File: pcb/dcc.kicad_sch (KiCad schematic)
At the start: 7 parts, among them J3 Screw_Terminal_01x08, J4 Screw_Terminal_01x02, U3 6N137, U4 LM339, U5 LM339, U6 LM339, U7 LM339

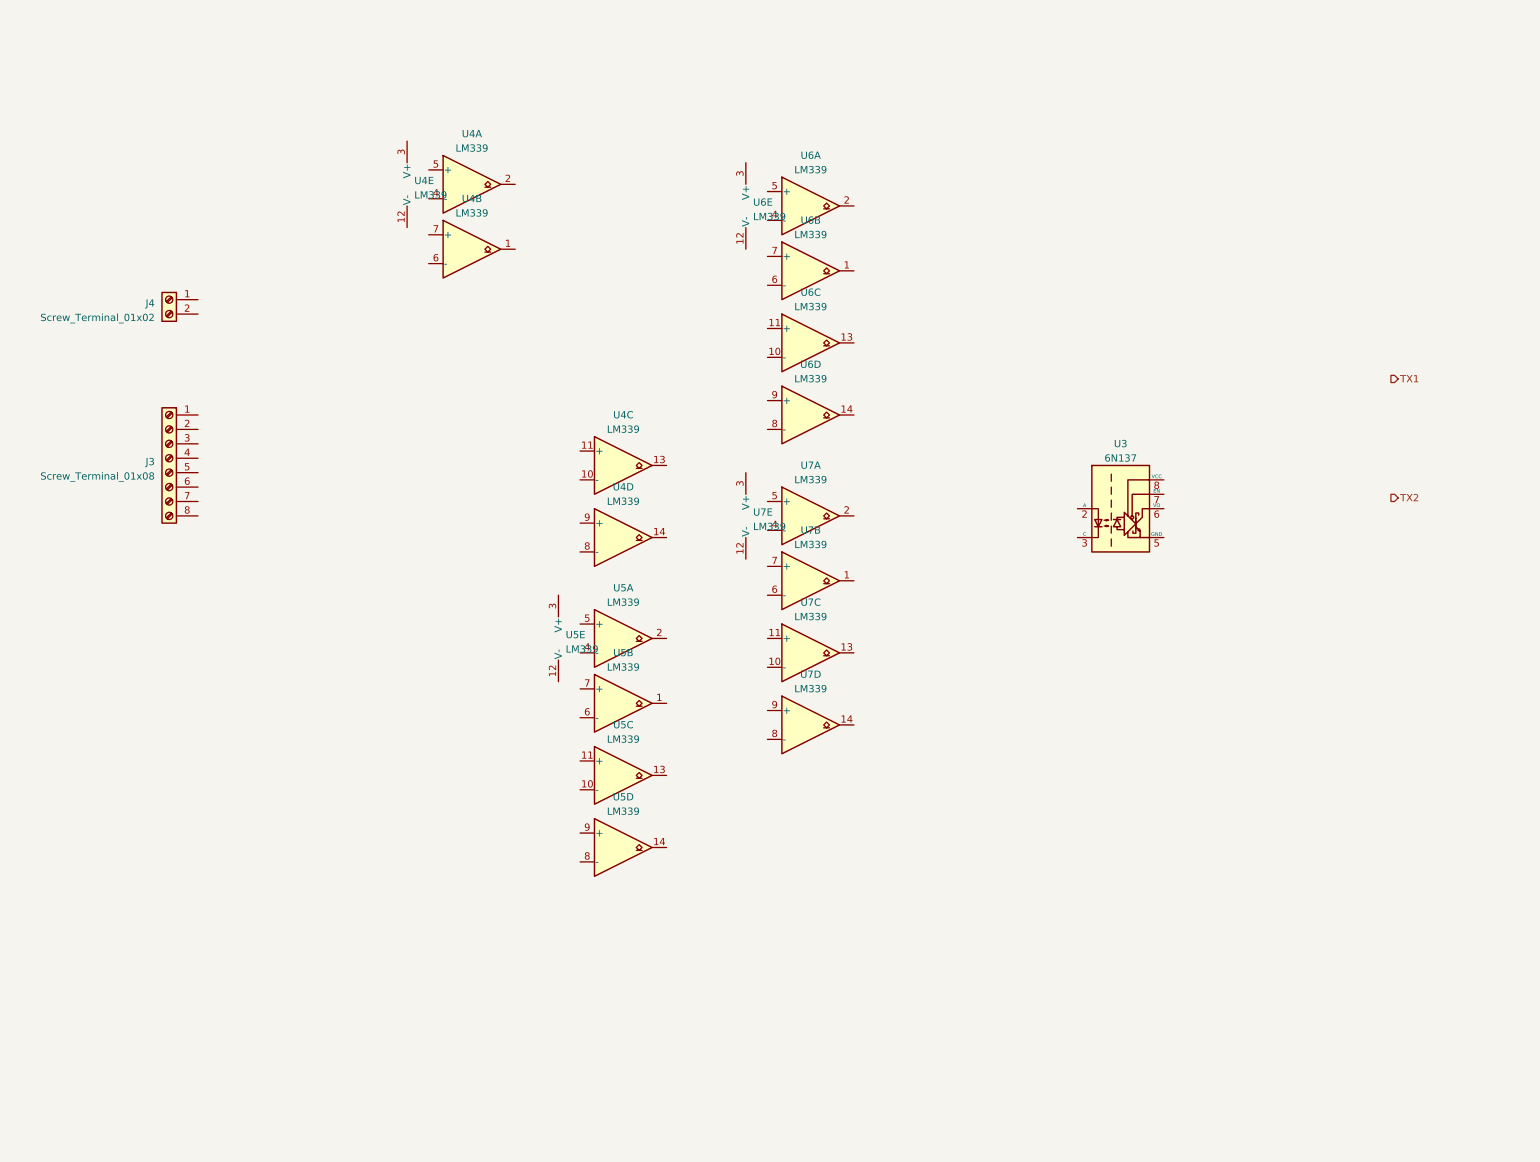
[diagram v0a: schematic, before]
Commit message: Wires adresses, add capacitors to MCU.
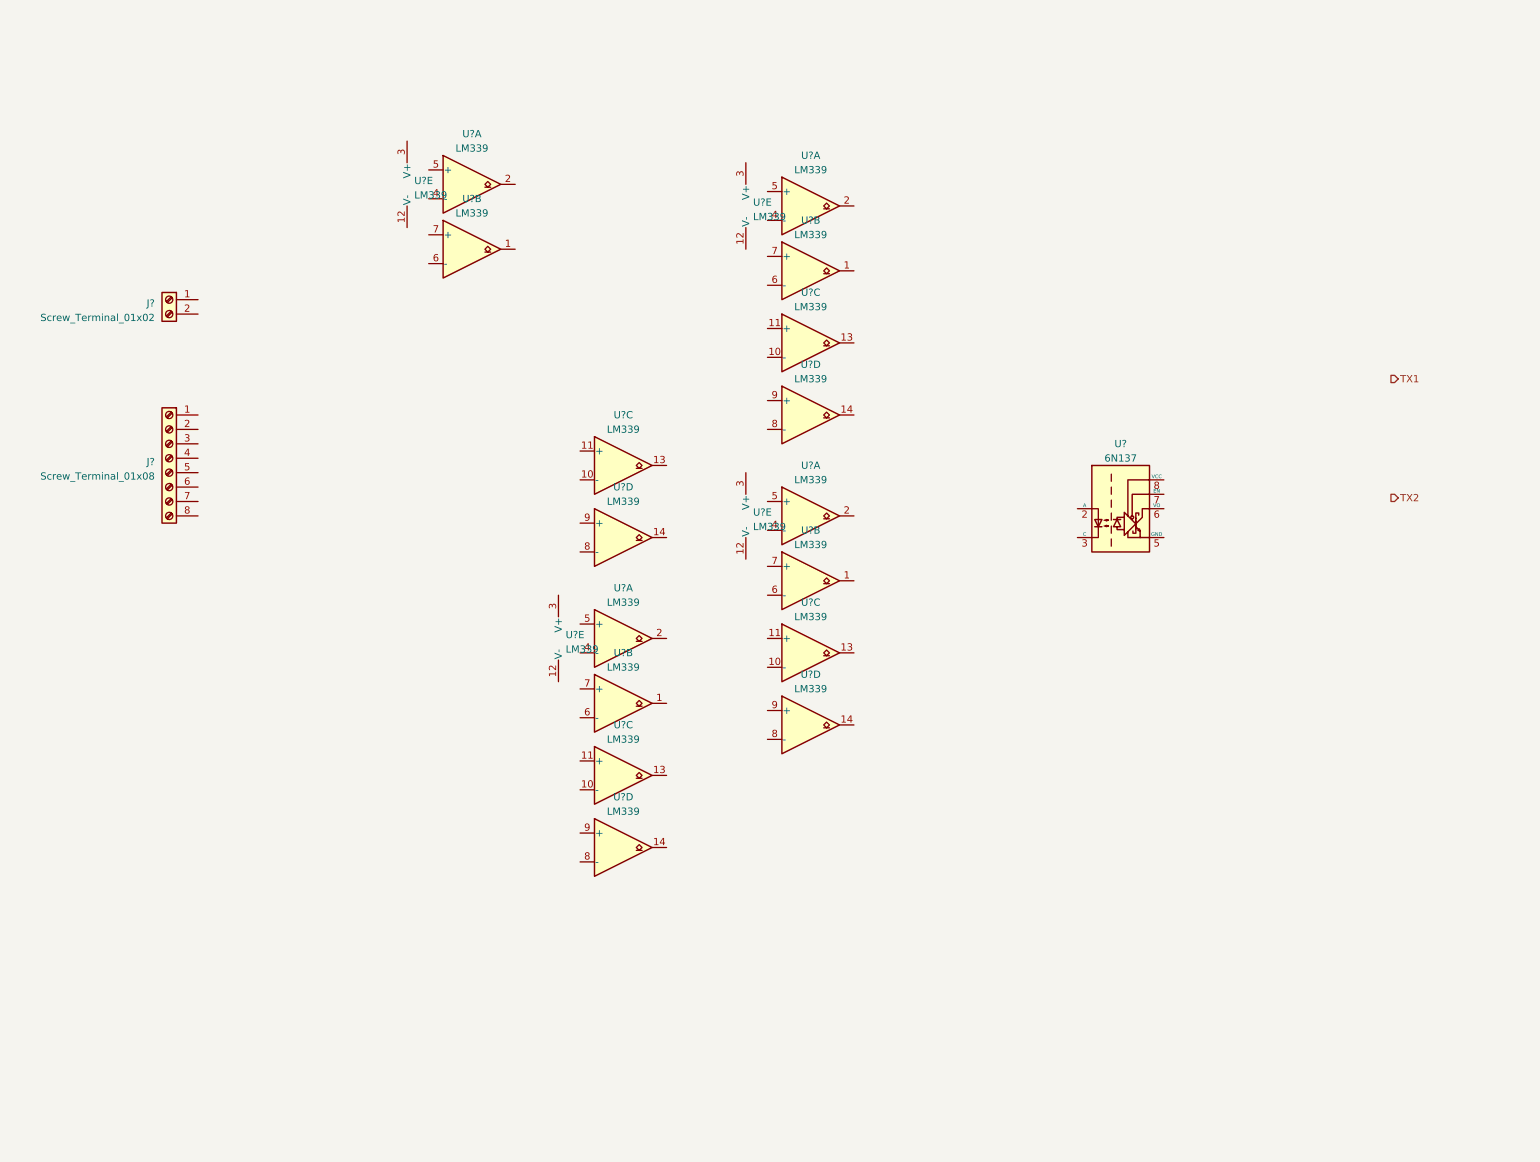
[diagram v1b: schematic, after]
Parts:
- renumbered J3 to J?, J4 to J?, U7 to U?, U5 to U?, U6 to U?, U4 to U?, U3 to U?

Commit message: Finished MTB part.
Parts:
- gave numbers to parts that had none: 7

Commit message: DCC WIP.
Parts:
- removed J2: Screw_Terminal_01x02, symbol Connector:Screw_Terminal_01x02
- removed J3: Screw_Terminal_01x08, symbol Connector:Screw_Terminal_01x08
- removed U7: 6N137, Package_DIP:DIP-8_W7.62mm, symbol Isolator:6N137
- added C14: C, symbol Device:C
- added R10: 1k, symbol Device:R
- added R11: 10k, symbol Device:R
- added R7, R8, R9: 1R5, symbol Device:R
- added U7: 4052, symbol 4xxx:4052
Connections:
- net TX1: now also U7.13 (X)
- net TX2: now also U7.3 (Y)
- net at U3.2: now also U3.1, R11.2
- net RC1: now reaches U3.4 (-)
- net RC1: now also U3.7 (+), R10.2
- net REF+: now reaches U3.5 (+)
- net REF-: now reaches U3.6 (-)
- new net +5VA: R11.1
- new net GNDA: R7.2, R8.2, R9.2
- new net J1: R10.1, R7.1
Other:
- note added: "Někde zde bude stabilizace napájení"
- moved on the sheet: U3A, U3B, U3C, U3D, U3E, U4A, U4B, U4C, U4D, U4E, U5A, U5B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

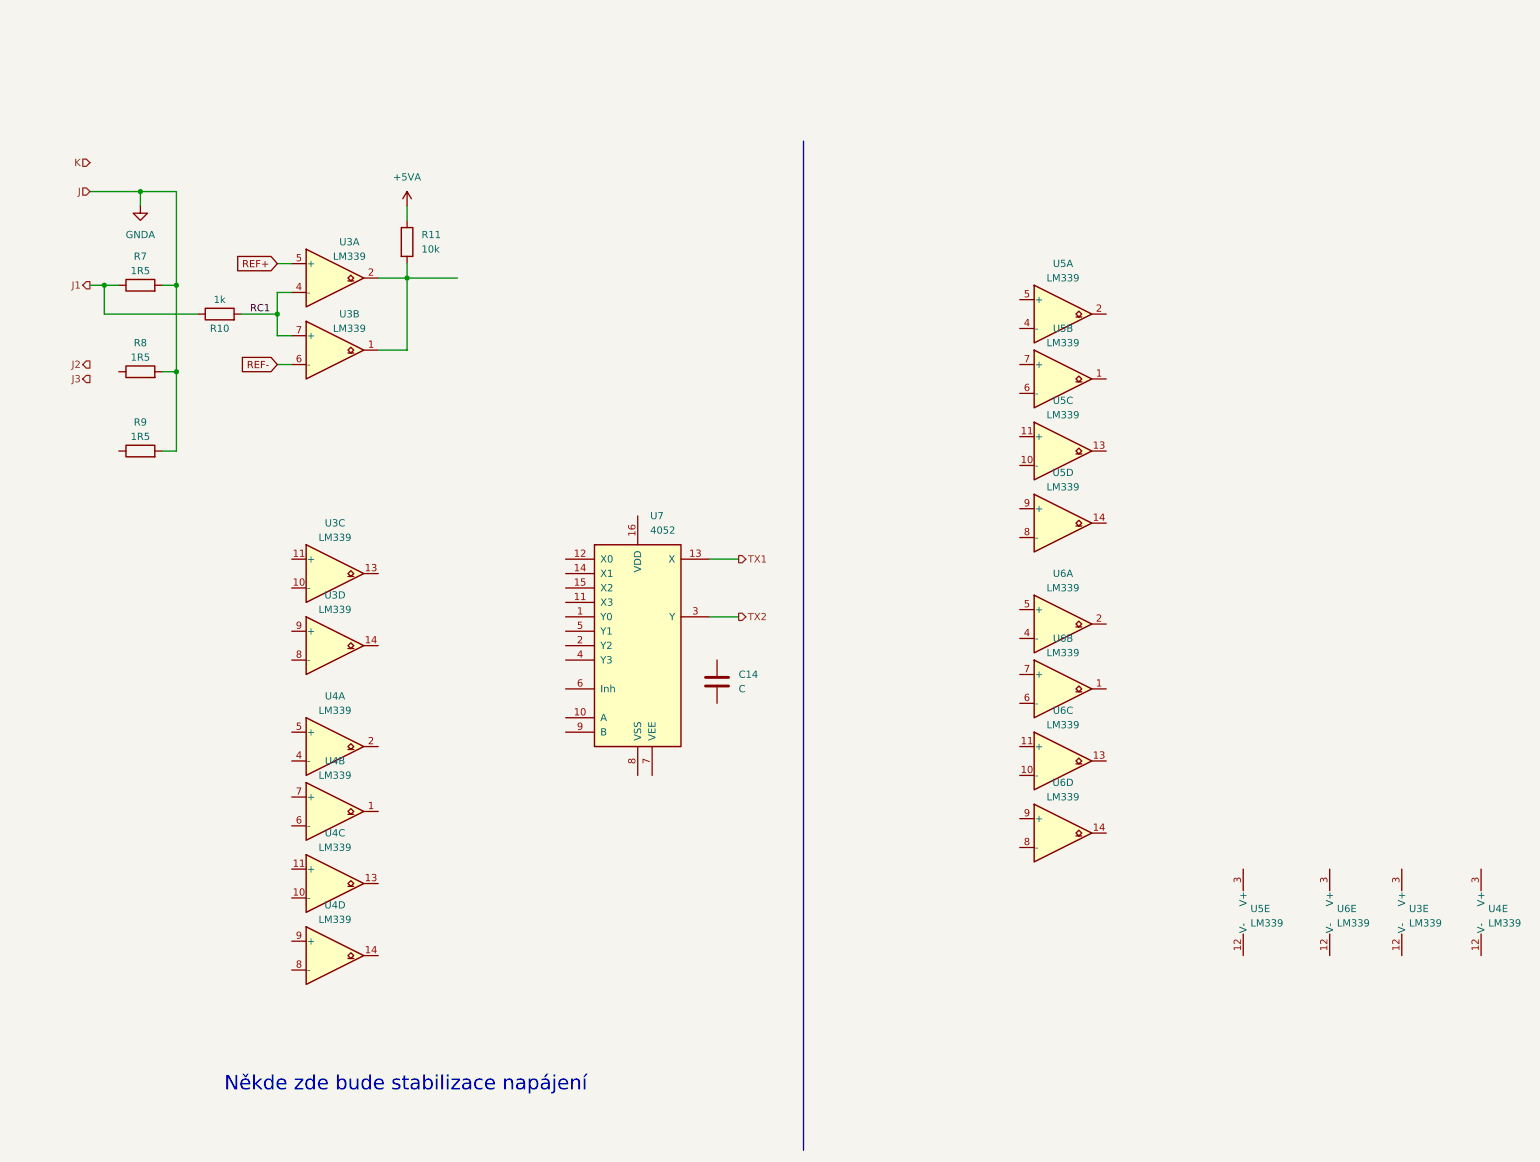
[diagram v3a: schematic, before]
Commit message: Some adjustments with comparators.
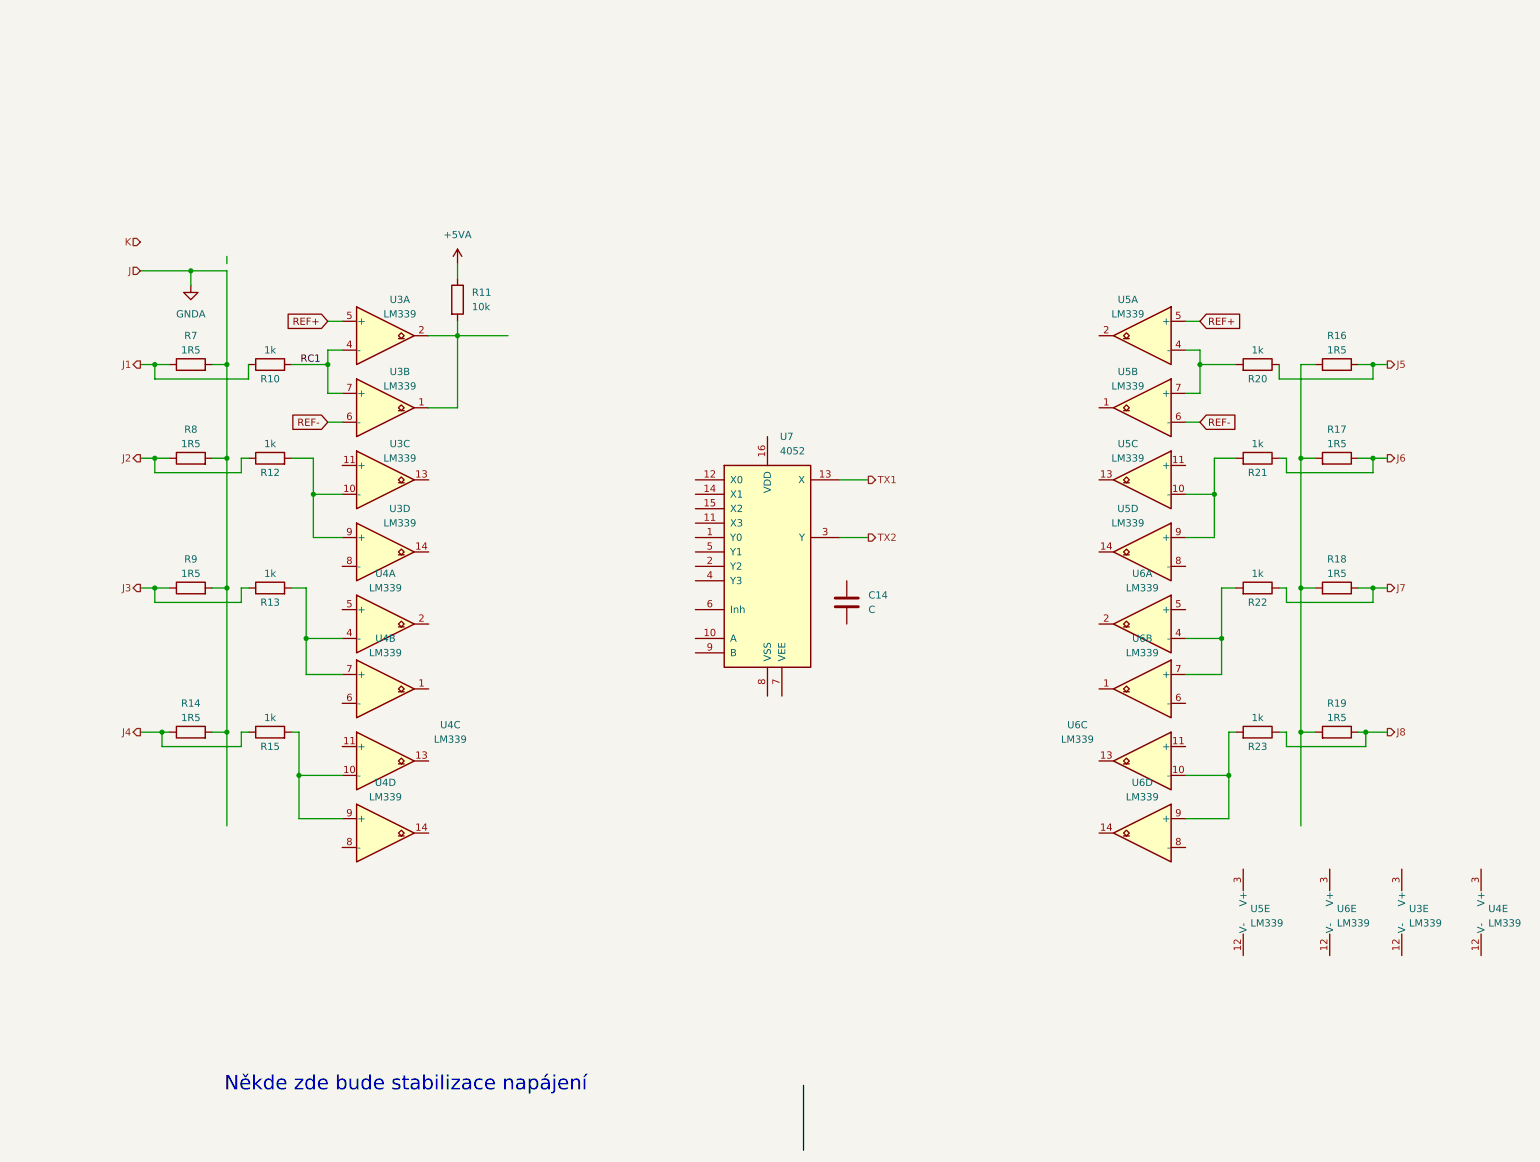
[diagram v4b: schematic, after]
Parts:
- added R12, R13, R15, R20, R21, R22, R23: 1k, symbol Device:R
- added R14, R16, R17, R18, R19: 1R5, symbol Device:R
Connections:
- net GNDA: now also R14.2
- net J2: now also R8.1, R12.1
- net J3: now also R9.1, R13.1
- net REF+: now also U5.5 (+)
- net REF-: now also U5.6 (-)
- net at U6.9 (+): now also U6.10 (-), R23.2
- net at U4.7 (+): now also U4.4 (-), R13.2
- net at U5.4 (-): now also U5.7 (+), R20.2
- net at U6.4 (-): now also U6.7 (+), R22.2
- net at U4.9 (+): now also U4.10 (-), R15.2
- net at U5.10 (-): now also U5.9 (+), R21.2
- net at U3.10 (-): now also U3.9 (+), R12.2
- new net: R16.2, R17.2, R18.2, R19.2
- new net J4: R14.1, R15.1
- new net J5: R16.1, R20.1
- new net J6: R17.1, R21.1
- new net J7: R18.1, R22.1
- new net J8: R19.1, R23.1
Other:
- moved on the sheet: C14, R10, R11, R7, R8, R9, U3A, U3B, U3C, U3D, U4A, U4B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

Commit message: Updated DCC part.
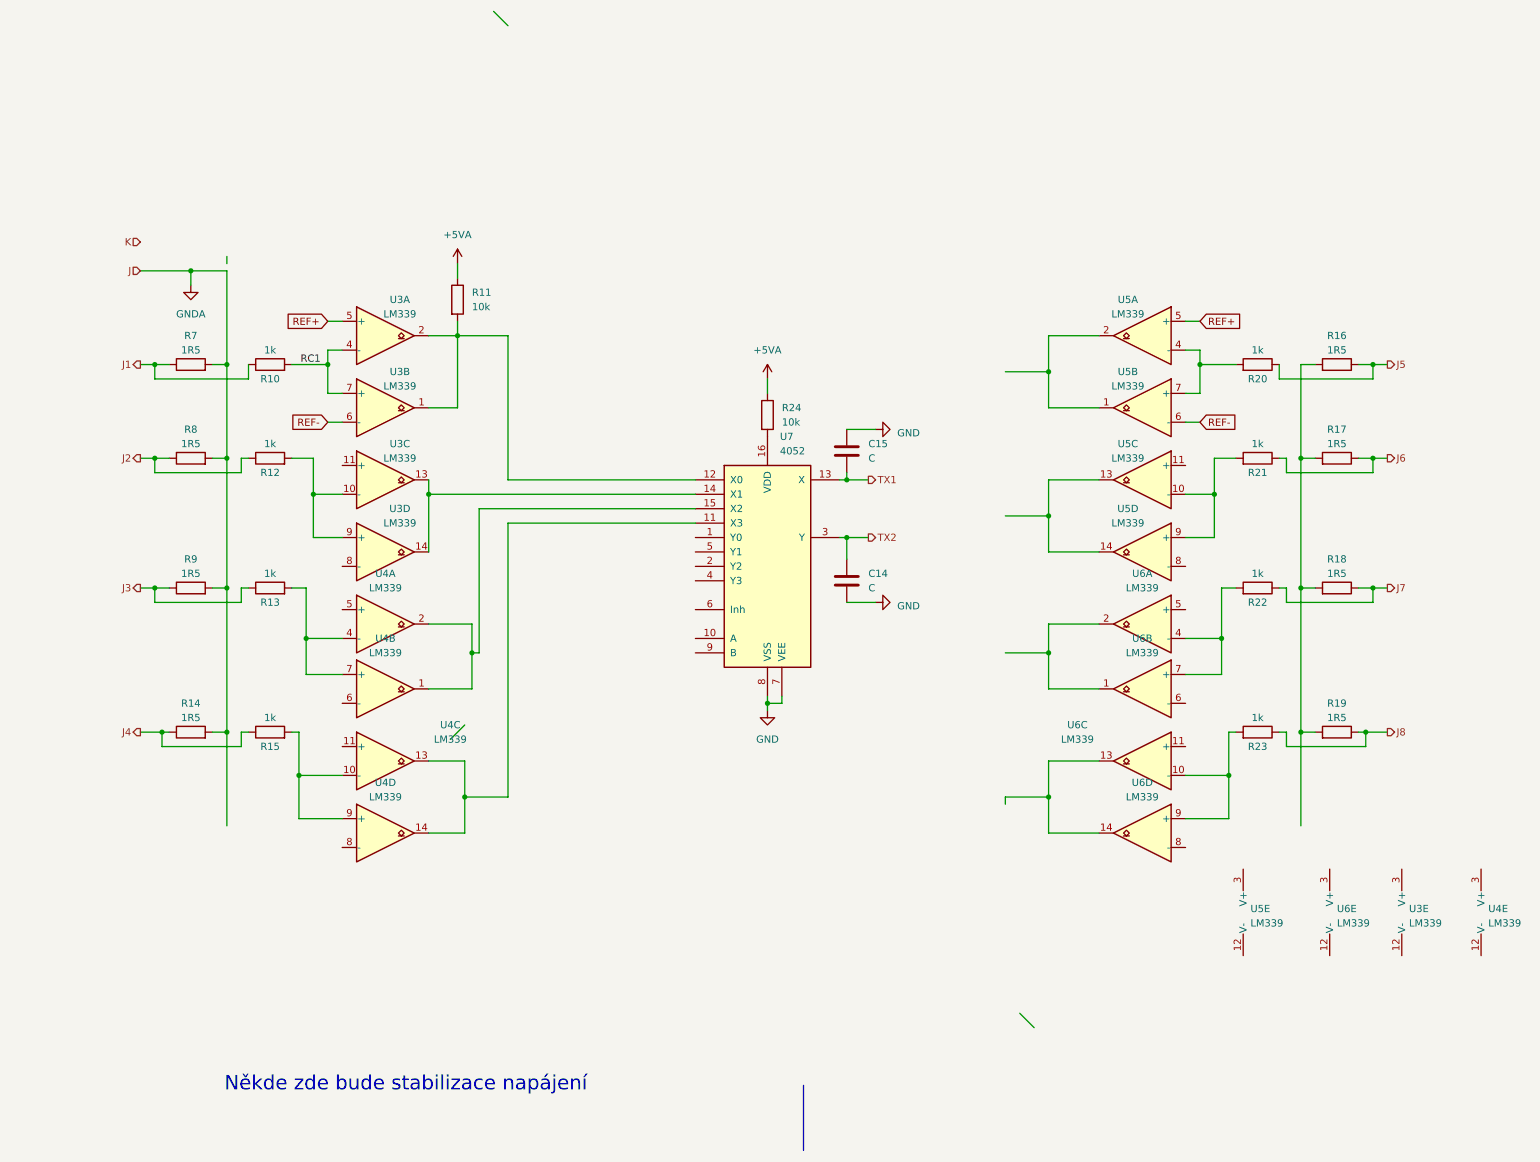
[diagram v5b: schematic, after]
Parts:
- added C15: C, symbol Device:C
- added R24: 10k, symbol Device:R
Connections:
- net +5VA: now also R24.1
- net TX1: now also C15.2
- net TX2: now also C14.1
- net at U4.1: now also U4.2, U7.15 (X2)
- net at U5.2: now also U5.1
- net at U5.13: now also U5.14
- net GND: now reaches C14.2
- net GND: now also U7.7 (VEE), U7.8 (VSS), C15.1
- net at U6.13: now also U6.14
- net at R11.2, U3.1, U3.2: now also U7.12 (X0)
- net at U4.14: now also U4.13, U7.11 (X3)
- net at U6.1: now also U6.2
- net at U3.13: now also U3.14, U7.14 (X1)
- net at U7.16 (VDD): now also R24.2
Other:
- moved on the sheet: C14
